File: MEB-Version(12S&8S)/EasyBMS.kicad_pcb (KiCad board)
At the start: 2 copper layers, 48.8 x 100 mm, 174 parts, among them IC1 XL7046, IC2 LTC6811IG-1#PBF, IC3 ISO1042DWV, IC4 AMS1117-3.3, J1 TYPE-C-31-M-12, Q14 CJ2301, Q15 CJ2301, Q16 CJ2301, Q18 CJ2301, Q20 CJ2301, Q22 CJ2301, Q24 CJ2301, Q26 CJ2301, Q28 CJ2301, Q30 CJ2301, Q32 CJ2301, Q34 CJ2301, U1 ESP32-C6-MINI-1-N4, Y1 FC-135_32.7680KA-A5

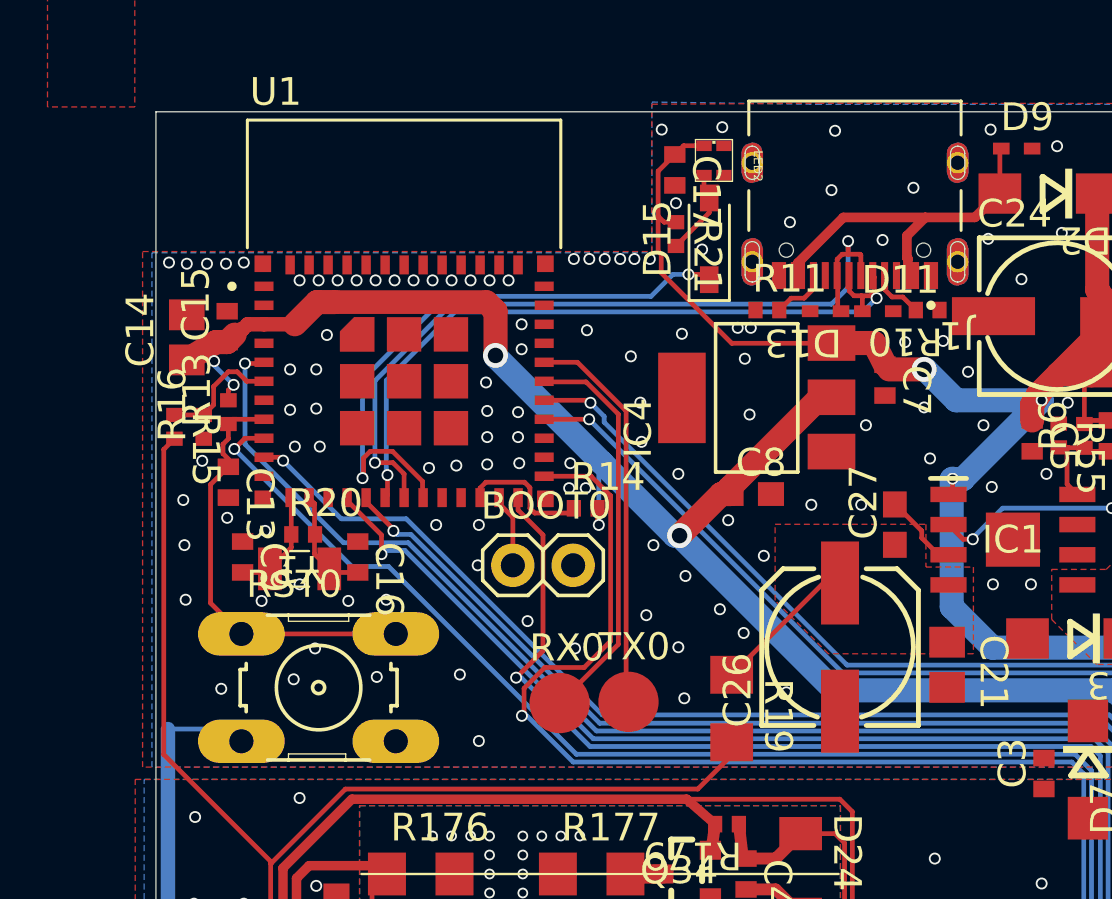
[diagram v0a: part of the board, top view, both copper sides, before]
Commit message: change to correct footprints, add LCSC numbers to schematic
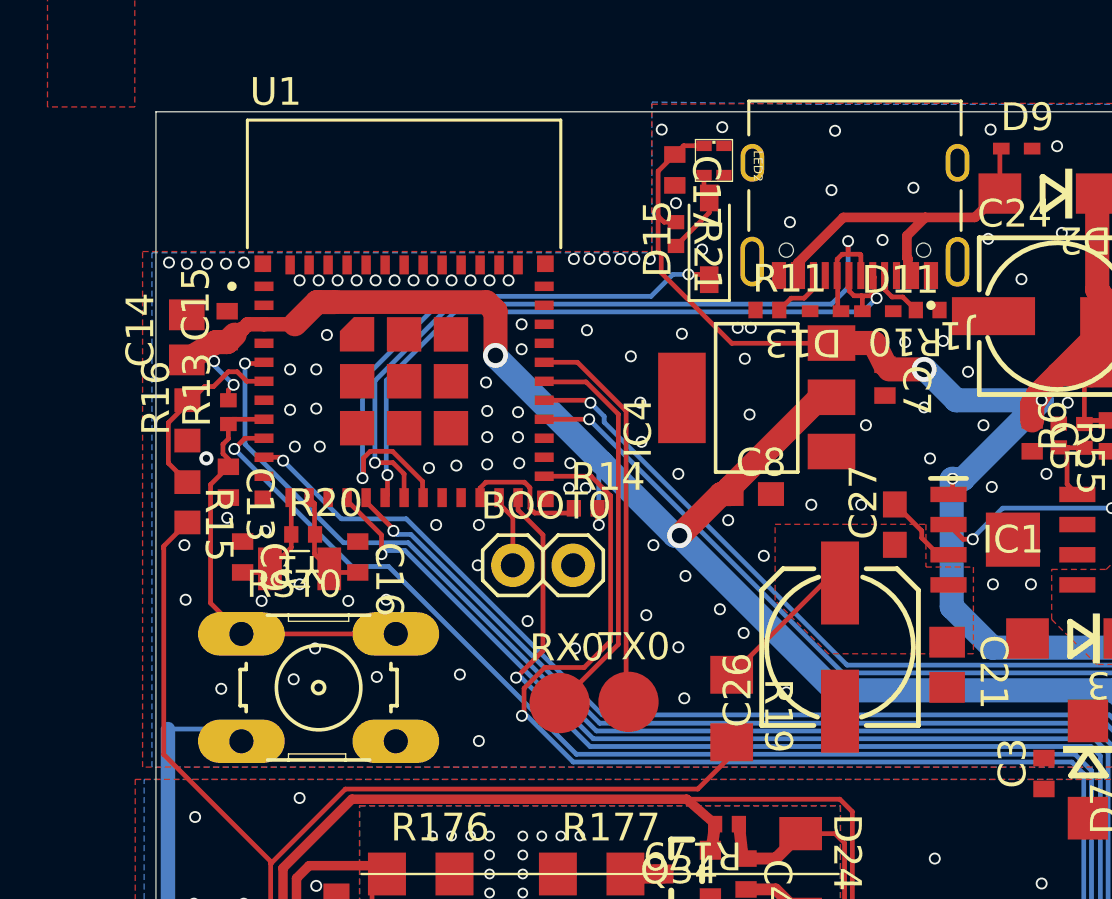
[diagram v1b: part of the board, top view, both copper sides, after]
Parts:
- R15, R16: footprint EasyBMS:R0402_334 -> EasyBMS:R0603_334
- moved R15 3.22 mm to (125.4, 71.5)
- moved R16 0.74 mm to (125.4, 68.0)
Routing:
- net /C12+POWER: track 67.8 -> 64.5 mm
- net /MODULEVOLTAGE: track 5.15 -> 7.91 mm
- net GND: vias 121 -> 120

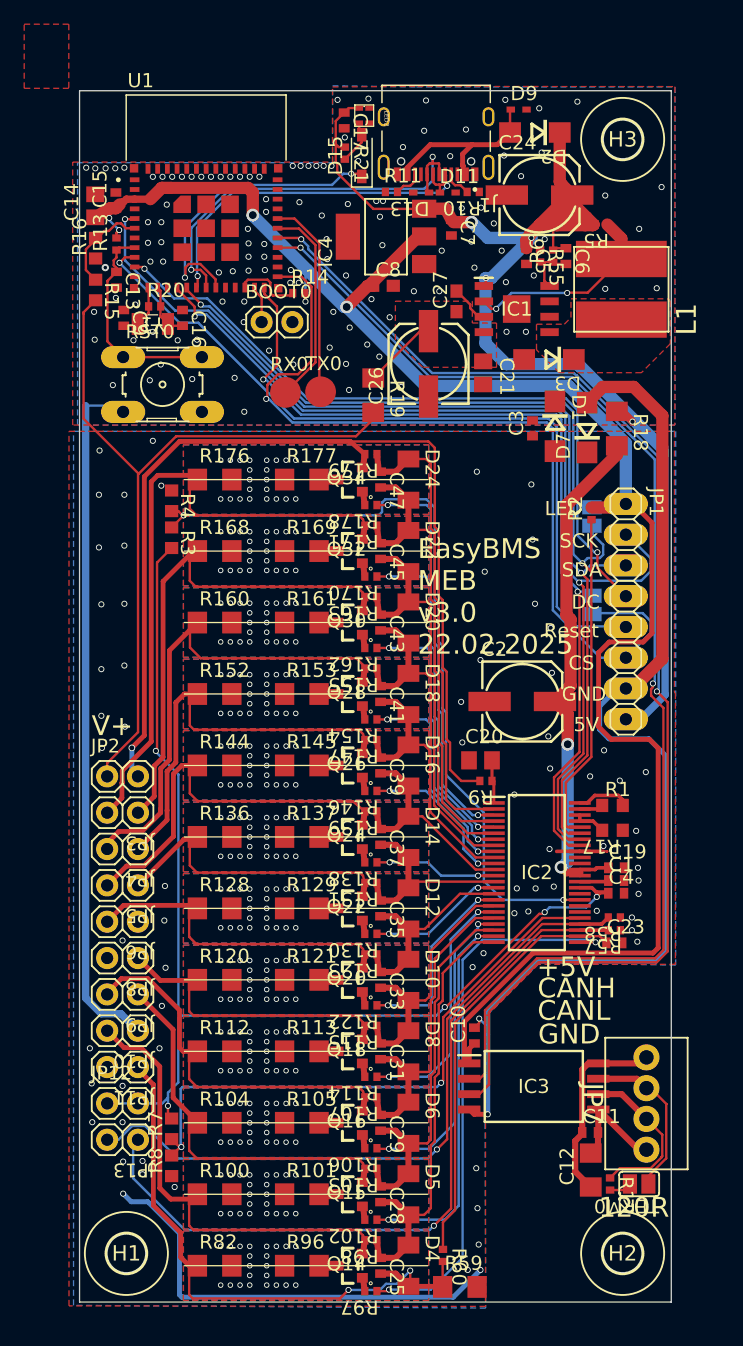
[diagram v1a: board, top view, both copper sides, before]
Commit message: change DRC rules to JLC capabilities and solve DRC errors
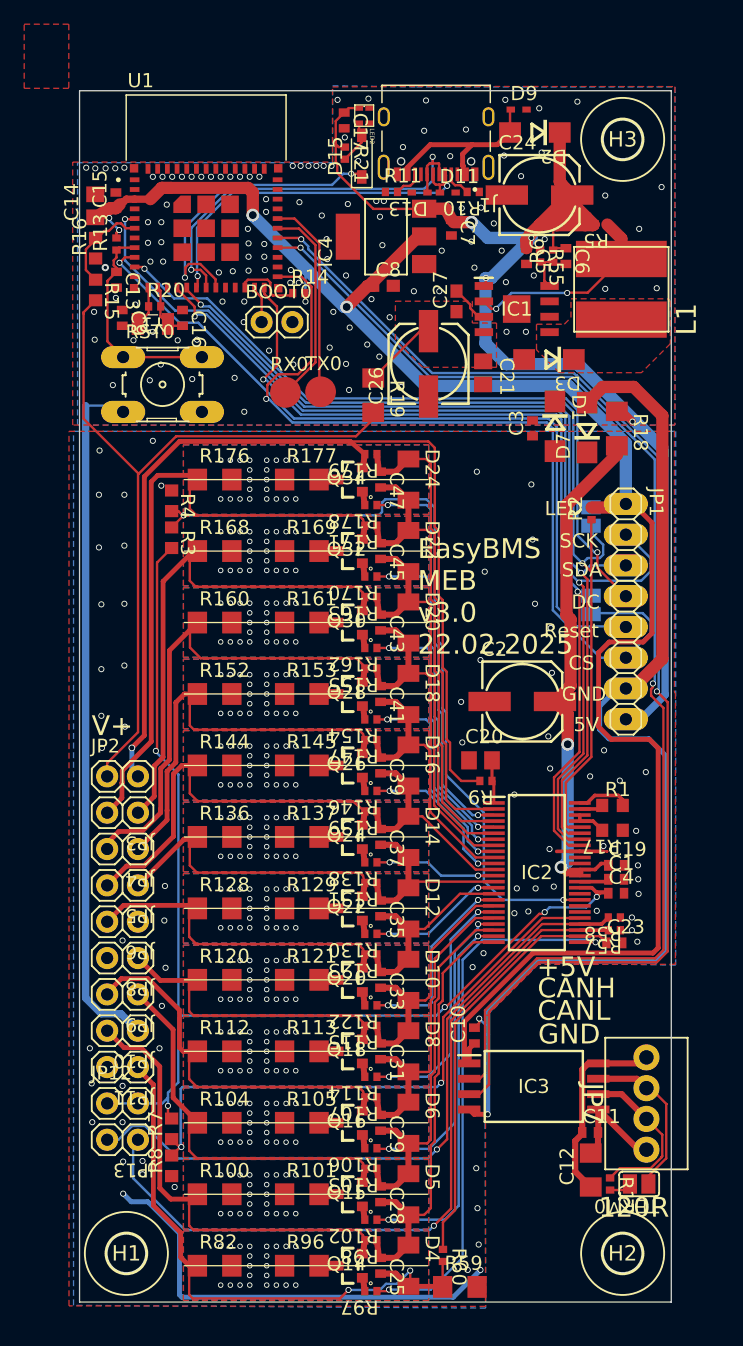
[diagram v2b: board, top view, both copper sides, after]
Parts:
- moved C19 0.20 mm to (168.4, 119.0)
- moved C9 0.13 mm to (127.6, 73.8)
- moved D13 0.13 mm to (152.2, 63.4)
- moved C1 0.10 mm to (168.4, 120.1)
- moved CSLTC0 0.08 mm to (166.3, 97.5)
- moved MISO0 0.08 mm to (166.3, 90.2)
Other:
- rule pad_to_mask_clearance: 0 -> 0.1016
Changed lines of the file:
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@@
 	)
 	(setup
-		(pad_to_mask_clearance 0)
-		(allow_soldermask_bridges_in_footprints no)
+		(stackup
+			(layer "F.SilkS"
+				(type "Top Silk Screen")
+			)
+			(layer "F.Paste"
+				(type "Top Solder Paste")
+			)
+			(layer "F.Mask"
+				(type "Top Solder Mask")
+				(thickness 0.01)
+			)
+			(layer "F.Cu"
+				(type "copper")
+				(thickness 0.035)
+			)
+			(layer "dielectric 1"
+				(type "core")
+				(thickness 1.51)
+				(material "FR4")
+				(epsilon_r 4.5)
+				(loss_tangent 0.02)
+			)
+			(layer "B.Cu"
+				(type "copper")
+				(thickness 0.035)
+			)
+			(layer "B.Mask"
+				(type "Bottom Solder Mask")
+				(thickness 0.01)
+			)
+			(layer "B.Paste"
+				(type "Bottom Solder Paste")
+			)
+			(layer "B.SilkS"
+				(type "Bottom Silk Screen")
+			)
+			(copper_finish "None")
+			(dielectric_constraints no)
+		)
+		(pad_to_mask_clearance 0.1016)
+		(allow_soldermask_bridges_in_footprints yes)
 		(tenting front back)
 		(pcbplotparams
@@
 	(footprint "EasyBMS:SOD3715X135_16378169"
 		(layer "F.Cu")
-		(at 147.3761 60.3536 90)
+		(at 147.3761 60.4 90)
 		(descr "SOD, 3.70 mm span, 2.70 X 1.55 X 1.35 mm body\n\nSOD package with 3.70 mm span with body size 2.70 X 1.55 X 1.35 mm")
 		(property "Reference" "D15"
@@
 	(footprint "EasyBMS:SOD523_210"
 		(layer "F.Cu")
-		(at 152.3261 63.4036 180)
+		(at 152.2 63.4036 180)
 		(descr "DIODE")
 		(property "Reference" "D13"
@@
 	(footprint "EasyBMS:C0402_334"
 		(layer "F.Cu")
-		(at 127.7261 73.7536 -90)
+		(at 127.6 73.7536 -90)
 		(descr "CAPACITOR")
 		(property "Reference" "C9"
@@
 	(footprint "EasyBMS:C0402_334"
 		(layer "F.Cu")
-		(at 168.3761 120.2036)
+		(at 168.3761 120.1)
 		(descr "CAPACITOR")
 		(property "Reference" "C1"
@@
 	(footprint "EasyBMS:C0402_334"
 		(layer "F.Cu")
-		(at 168.3761 119.1536)
+		(at 168.3761 118.95)
 		(descr "CAPACITOR")
 		(property "Reference" "C19"
@@
 		(at 147.5761 57.0536 -90)
 		(property "Reference" "LED2"
-			(at -0.43 -1.63 270)
+			(at 1.0464 -0.4239 270)
 			(unlocked yes)
 			(layer "F.SilkS")
@@
 	(footprint "EasyBMS:SJ_252"
 		(layer "B.Cu")
-		(at 166.3761 90.1536 90)
+		(at 166.3 90.1536 90)
 		(descr "Solder jumper")
 		(property "Reference" "MISO0"
@@
 	(footprint "EasyBMS:SJ_252"
 		(layer "B.Cu")
-		(at 166.3761 97.4536 -90)
+		(at 166.3 97.4536 -90)
 		(descr "Solder jumper")
 		(property "Reference" "CSLTC0"
@@
 	)
 	(via
-		(at 149.1261 64.1036)
+		(at 149.2 64.1036)
 		(size 0.5024)
 		(drill 0.35)
@@
 	)
 	(via
-		(at 170.1761 119.1536)
+		(at 170.1761 118.95)
 		(size 0.5024)
 		(drill 0.35)
@@
 	)
 	(via
-		(at 170.2261 120.2036)
+		(at 170.2 120.1)
 		(size 0.5024)
 		(drill 0.35)
@@
 	)
 	(segment
+		(start 165.3779 119.296)
+		(end 166.6337 119.296)
+		(width 0.3)
+		(layer "F.Cu")
+		(net 80)
+	)
+	(segment
 		(start 168.4311 85.046625)
 		(end 168.4311 84.3154)
@@
 	)
 	(segment
+		(start 167.1297 118.8)
+		(end 167.7261 118.8)
+		(width 0.3)
+		(layer "F.Cu")
+		(net 80)
+	)
+	(segment
 		(start 164.2759 119.5536)
 		(end 165.3779 119.5536)
@@
 	)
 	(segment
+		(start 166.6337 119.296)
+		(end 167.1297 118.8)
+		(width 0.3)
+		(layer "F.Cu")
+		(net 80)
+	)
+	(segment
 		(start 163.3273 105.4246)
 		(end 164.3761 106.4734)
@@
 		(net 80)
 	)
-	(segment
-		(start 166.6337 119.296)
-		(end 166.7761 119.1536)
-		(width 0.3)
-		(layer "F.Cu")
-		(net 80)
-	)
-	(segment
-		(start 165.3779 119.296)
-		(end 166.6337 119.296)
-		(width 0.3)
-		(layer "F.Cu")
-		(net 80)
-	)
-	(segment
-		(start 166.7761 119.1536)
-		(end 167.7261 119.1536)
-		(width 0.3)
-		(layer "F.Cu")
-		(net 80)
-	)
 	(via
 		(at 164.3761 108.9536)
@@
 			(clearance 0.4)
 		)
-		(min_thickness 0.0635)
+		(min_thickness 0.127)
 		(filled_areas_thickness no)
 		(fill yes
@@
 			(clearance 0.254)
 		)
-		(min_thickness 0.0635)
+		(min_thickness 0.127)
 		(filled_areas_thickness no)
 		(fill yes
@@
 			(clearance 0.254)
 		)
-		(min_thickness 0.0635)
+		(min_thickness 0.127)
 		(filled_areas_thickness no)
 		(fill yes
@@
 			(clearance 0.4)
 		)
-		(min_thickness 0.0635)
+		(min_thickness 0.127)
 		(filled_areas_thickness no)
 		(fill yes

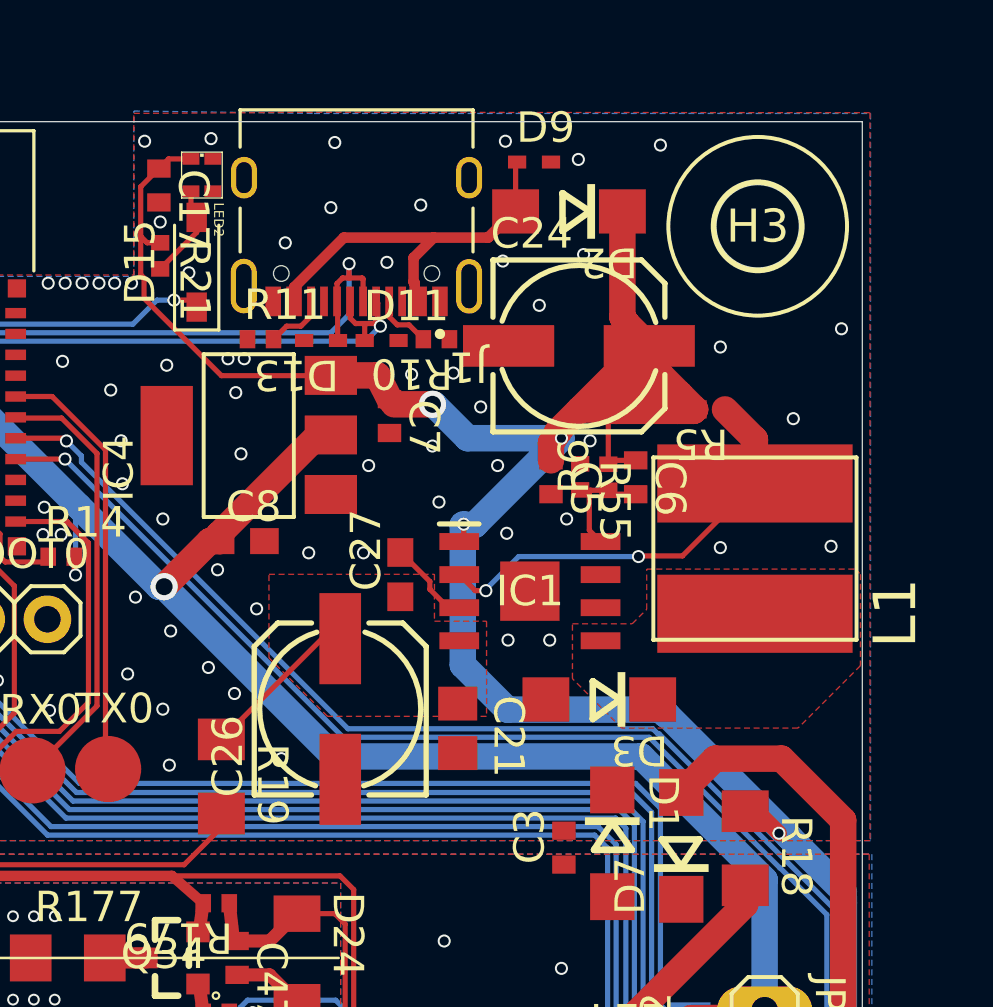
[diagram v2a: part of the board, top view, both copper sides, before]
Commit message: fixed wrong footprints and symbols, connect 3d models with footprints
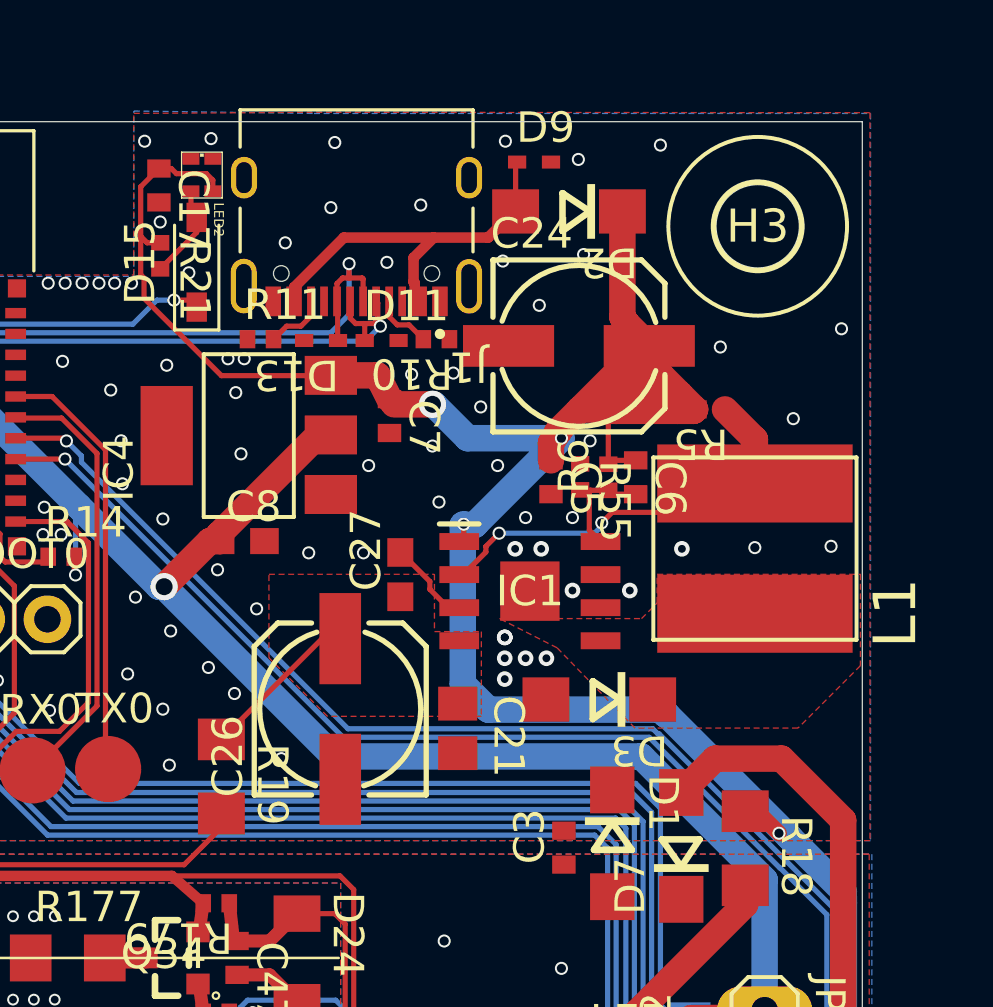
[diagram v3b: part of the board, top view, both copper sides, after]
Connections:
- IC1 pad 9: GND -> Net-(IC1-SW)
- IC4 pad 4: (no net) -> unconnected-(IC4-Pad4)
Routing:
- net +5V/1: track 110.8 -> 112.5 mm
- net GND: vias 120 -> 129
